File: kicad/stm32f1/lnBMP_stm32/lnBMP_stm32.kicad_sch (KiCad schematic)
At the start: 26 parts, among them J1 BMP Debug1, J2 BMP Debug2, J3 Debug port, J4 USB_OTG, U1 STM32F103CBTx, U2 LM1117-3.3, Y1 Crystal

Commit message: kicad : Update ch32 and stm32 pcbs
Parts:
- added DFU1: SW_DIP_x01, Button_Switch_SMD:SW_SPST_CK_RS282G05A3, symbol Switch:SW_DIP_x01
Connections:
- net NRESET is gone; now on net GND: J3.5 (Pin_5)
- net GND: now also DFU1.2; no longer J3.1 (Pin_1)
- net IN_FORCE_DFU: now also DFU1.1
- net SWDCLK: now also J3.4 (Pin_4); no longer J3.2 (Pin_2)
- net UART_TX: now also J3.2 (Pin_2); no longer J3.4 (Pin_4)
- net NRST: now reaches C1.1, R2.2, RST1.1, U1.7 (NRST)
- net NRST: now also J3.1 (Pin_1)
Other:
- moved on the sheet: J3
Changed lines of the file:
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@@
   (junction (at 265.43 24.13) (diameter 0) (color 0 0 0 0)
   )
+  (junction (at 50.8 62.23) (diameter 0) (color 0 0 0 0)
+  )
   (junction (at 252.73 31.75) (diameter 0) (color 0 0 0 0)
   )
@@
   (junction (at 74.93 62.23) (diameter 0) (color 0 0 0 0)
   )
+  (junction (at 48.26 130.81) (diameter 0) (color 0 0 0 0)
+  )
   (junction (at 13.97 72.39) (diameter 0) (color 0 0 0 0)
   )
@@
     (stroke (width 0) (type default))
   )
+  (wire (pts (xy 48.26 130.81) (xy 48.26 134.62))
+    (stroke (width 0) (type default))
+  )
   (wire (pts (xy 252.73 31.75) (xy 265.43 31.75))
     (stroke (width 0) (type default))
@@
     (stroke (width 0) (type default))
   )
+  (wire (pts (xy 55.88 50.8) (xy 55.88 62.23))
+    (stroke (width 0) (type default))
+  )
   (wire (pts (xy 144.78 146.05) (xy 144.78 149.86))
     (stroke (width 0) (type default))
@@
     (stroke (width 0) (type default))
   )
+  (wire (pts (xy 50.8 62.23) (xy 50.8 67.31))
+    (stroke (width 0) (type default))
+  )
   (wire (pts (xy 48.26 74.93) (xy 48.26 77.47))
     (stroke (width 0) (type default))
@@
     (stroke (width 0) (type default))
   )
+  (wire (pts (xy 48.26 130.81) (xy 52.07 130.81))
+    (stroke (width 0) (type default))
+  )
   (wire (pts (xy 102.87 36.83) (xy 106.68 36.83))
     (stroke (width 0) (type default))
@@
     (stroke (width 0) (type default))
   )
-  (wire (pts (xy 50.8 43.18) (xy 50.8 67.31))
+  (wire (pts (xy 55.88 62.23) (xy 50.8 62.23))
+    (stroke (width 0) (type default))
+  )
+  (wire (pts (xy 50.8 43.18) (xy 50.8 62.23))
     (stroke (width 0) (type default))
   )
@@
     (stroke (width 0) (type default))
   )
+  (wire (pts (xy 48.26 149.86) (xy 48.26 151.13))
+    (stroke (width 0) (type default))
+  )
   (wire (pts (xy 85.09 100.33) (xy 91.44 100.33))
     (stroke (width 0) (type default))
@@
     (stroke (width 0) (type default))
   )
-  (wire (pts (xy 46.99 130.81) (xy 52.07 130.81))
-    (stroke (width 0) (type default))
+  (wire (pts (xy 46.99 130.81) (xy 48.26 130.81))
+    (stroke (width 0) (type default))
+  )
+  (global_label "NRST" (shape input) (at 55.88 50.8 90) (fields_autoplaced)
+    (effects (font (size 1.27 1.27)) (justify left))
+    (property "Intersheetrefs" "${INTERSHEET_REFS}" (at 55.88 43.0372 90)
+      (effects (font (size 1.27 1.27)) (justify left) hide)
+    )
   )
   (global_label "SWDCLK" (shape input) (at 106.68 105.41 0) (fields_autoplaced)
@@
     )
   )
-  (global_label "NRESET" (shape input) (at 137.16 149.86 270) (fields_autoplaced)
-    (effects (font (size 1.27 1.27)) (justify right))
-    (property "Intersheetrefs" "${INTERSHEET_REFS}" (at 137.0806 159.3488 90)
+  (global_label "NRST" (shape input) (at 137.16 149.86 270) (fields_autoplaced)
+    (effects (font (size 1.27 1.27)) (justify right))
+    (property "Intersheetrefs" "${INTERSHEET_REFS}" (at 137.16 157.6228 90)
       (effects (font (size 1.27 1.27)) (justify right) hide)
     )
@@
     )
   )
+  (symbol (lib_id "Switch:SW_DIP_x01") (at 48.26 142.24 270) (unit 1)
+    (in_bom yes) (on_board yes) (dnp no) (fields_autoplaced)
+    (property "Reference" "DFU1" (at 52.07 140.97 90)
+      (effects (font (size 1.27 1.27)) (justify left))
+    )
+    (property "Value" "SW_DIP_x01" (at 52.07 143.51 90)
+      (effects (font (size 1.27 1.27)) (justify left))
+    )
+    (property "Footprint" "Button_Switch_SMD:SW_SPST_CK_RS282G05A3" (at 48.26 142.24 0)
+      (effects (font (size 1.27 1.27)) hide)
+    )
+    (property "Datasheet" "~" (at 48.26 142.24 0)
+      (effects (font (size 1.27 1.27)) hide)
+    )
+    (pin "1")
+    (pin "2")
+    (instances
+      (project "lnBMP_stm32"
+        (path "/fbe443d6-6d74-4abc-9dee-16e0160553bc"
+          (reference "DFU1") (unit 1)
+        )
+      )
+    )
+  )
   (symbol (lib_id "power:GND") (at 213.36 41.91 0) (unit 1)
     (in_bom yes) (on_board yes) (dnp no) (fields_autoplaced)
@@
     )
   )
+  (symbol (lib_id "power:GND") (at 48.26 151.13 0) (unit 1)
+    (in_bom yes) (on_board yes) (dnp no) (fields_autoplaced)
+    (property "Reference" "#PWR03" (at 48.26 157.48 0)
+      (effects (font (size 1.27 1.27)) hide)
+    )
+    (property "Value" "GND" (at 48.26 156.21 0)
+      (effects (font (size 1.27 1.27)))
+    )
+    (property "Footprint" "" (at 48.26 151.13 0)
+      (effects (font (size 1.27 1.27)) hide)
+    )
+    (property "Datasheet" "" (at 48.26 151.13 0)
+      (effects (font (size 1.27 1.27)) hide)
+    )
+    (pin "1")
+    (instances
+      (project "lnBMP_stm32"
+        (path "/fbe443d6-6d74-4abc-9dee-16e0160553bc"
+          (reference "#PWR03") (unit 1)
+        )
+      )
+    )
+  )
   (symbol (lib_id "Device:R_Small") (at 38.1 38.1 0) (unit 1)
     (in_bom yes) (on_board yes) (dnp no) (fields_autoplaced)
@@
     )
   )
-  (symbol (lib_id "Connector:Conn_01x05_Male") (at 142.24 140.97 270) (unit 1)
+  (symbol (lib_id "Connector:Conn_01x05_Male") (at 142.24 140.97 90) (mirror x) (unit 1)
     (in_bom yes) (on_board yes) (dnp no)
     (property "Reference" "J3" (at 142.24 135.89 90)
@@
       (effects (font (size 1.27 1.27)))
     )
-    (property "Footprint" "Connector_JST:JST_XH_B5B-XH-A_1x05_P2.50mm_Vertical" (at 143.51 165.1 90)
-      (effects (font (size 1.27 1.27)))
-    )
+    (property "Footprint" "Connector_JST:JST_XH_B5B-XH-A_1x05_P2.50mm_Vertical" (at 140.97 165.1 90)
+      (effects (font (size 1.27 1.27)))
+    )

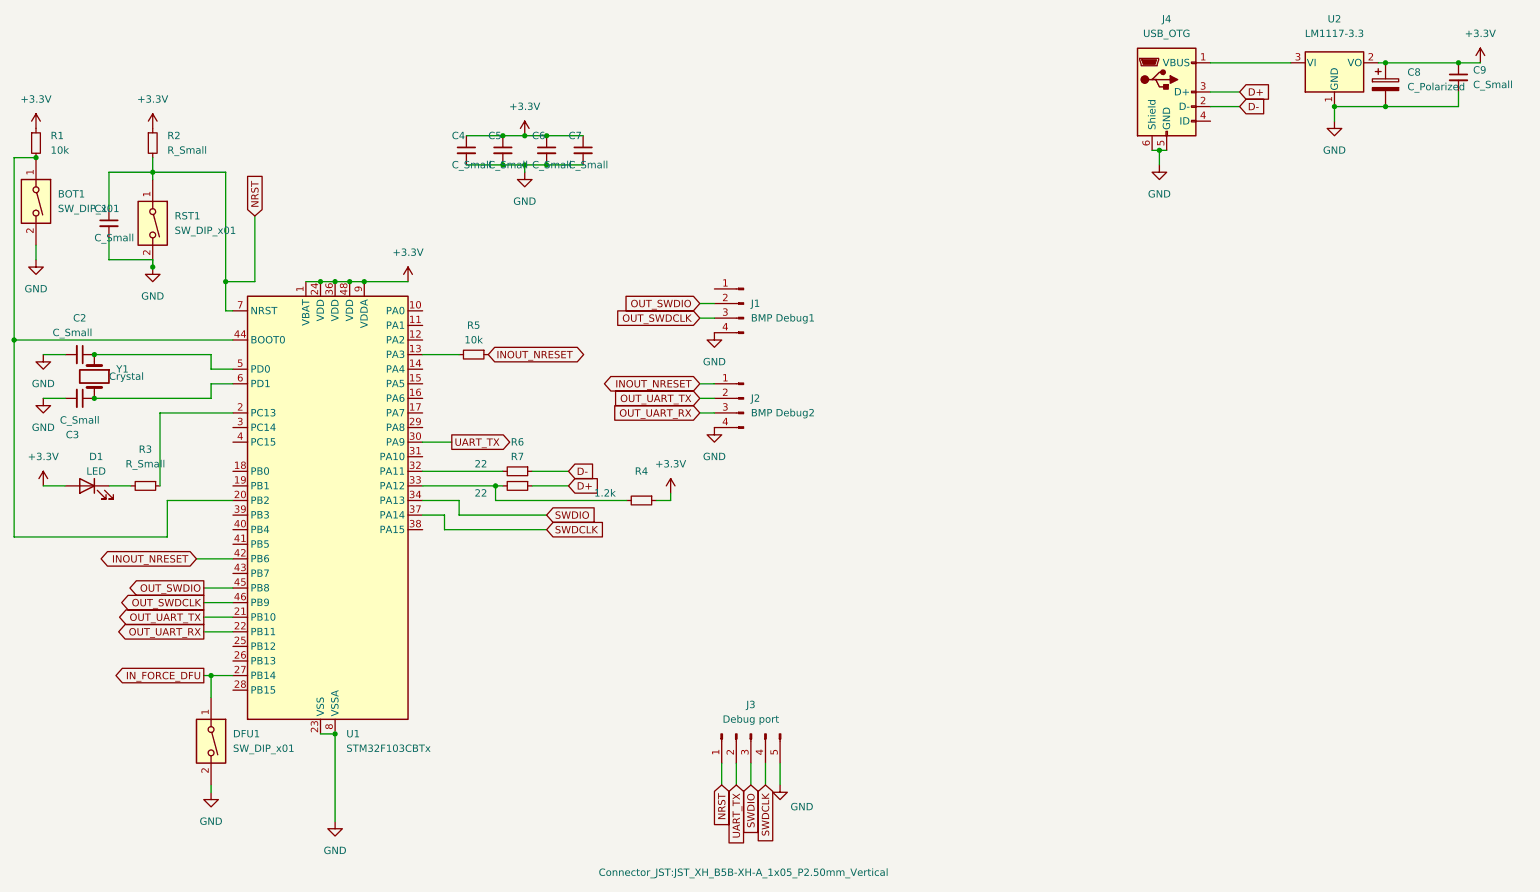
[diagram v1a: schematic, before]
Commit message: cleanup a bit the text + fix the inverted BOOT signal on stm32F1
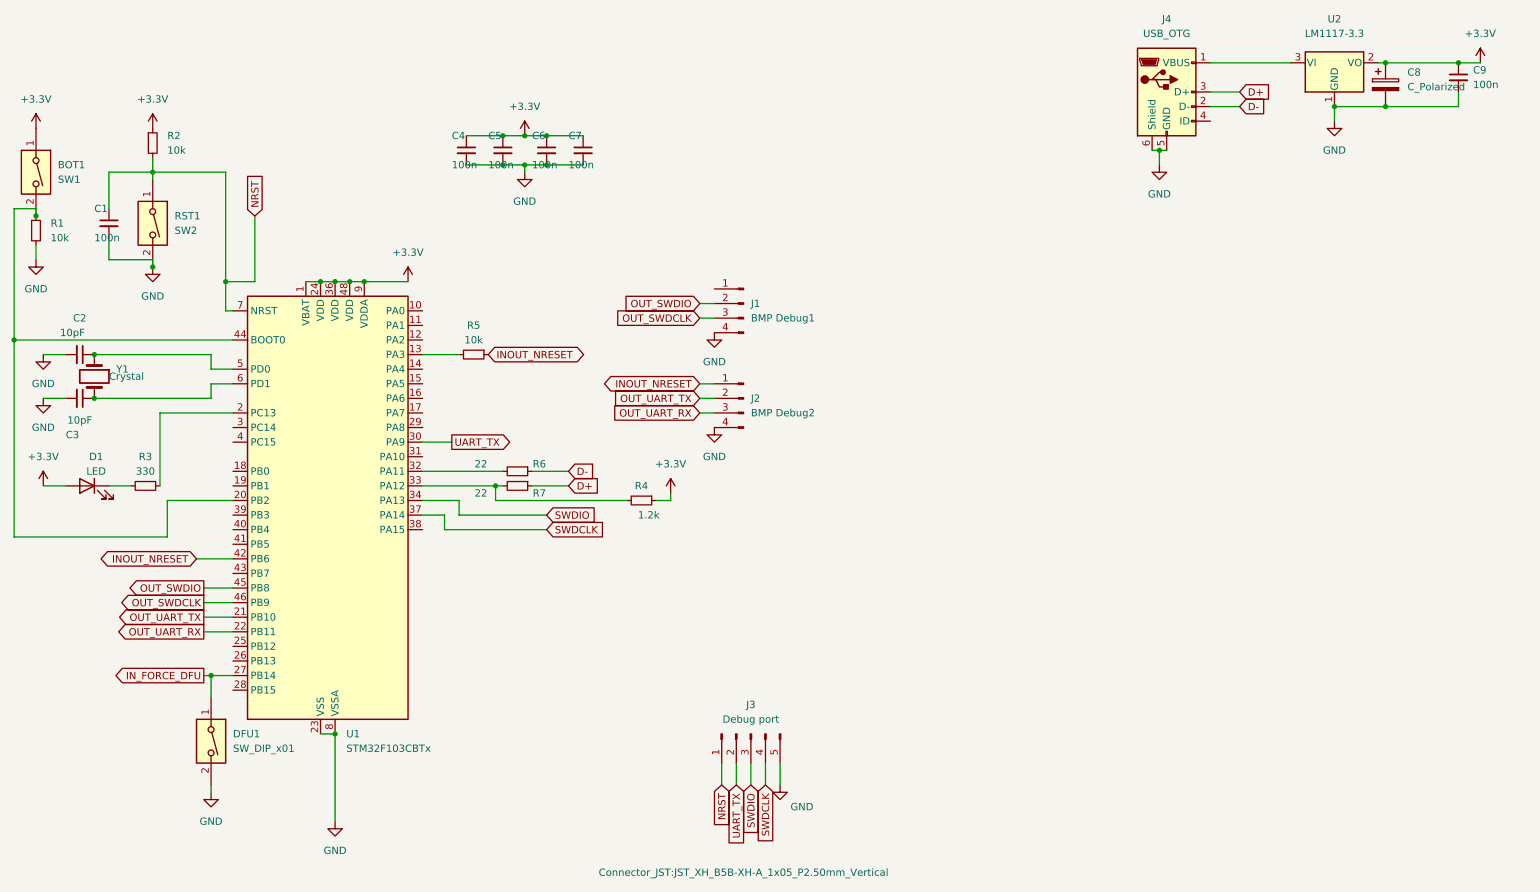
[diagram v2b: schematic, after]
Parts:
- BOT1: value SW_DIP_x01 -> SW1
- C1, C4, C5, C6, C7, C9: value C_Small -> 100n
- C2, C3: value C_Small -> 10pF
- R2: value R_Small -> 10k
- R3: value R_Small -> 330
- RST1: value SW_DIP_x01 -> SW2
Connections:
- net +3.3V: now also BOT1.1; no longer R1.1
- net GND: now also R1.2; no longer BOT1.2
- net at U1.20 (PB2), U1.44 (BOOT0): now also BOT1.2, R1.1; no longer BOT1.1, R1.2
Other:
- moved on the sheet: BOT1, R1

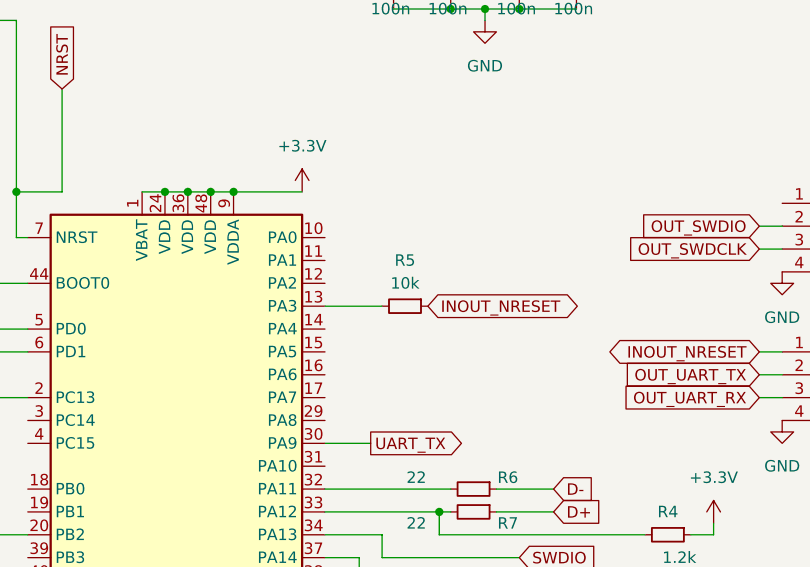
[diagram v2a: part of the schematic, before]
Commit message: stm32/gd32 : reduce rst input resistor, it acts as if a pulldown was behind
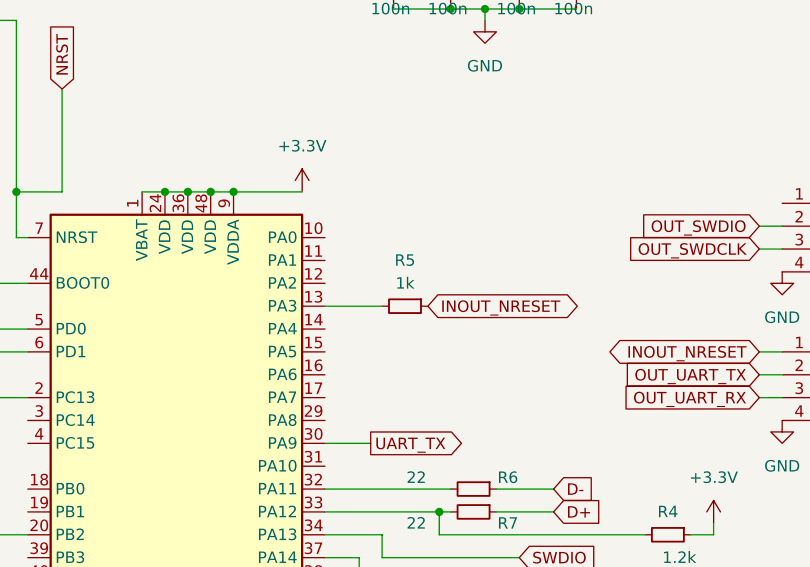
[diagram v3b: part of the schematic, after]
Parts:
- R5: value 10k -> 1k

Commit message: update lnArduino
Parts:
- added J5: Conn_ARM_JTAG_SWD_10, Connector_PinHeader_1.27mm:PinHeader_2x05_P1.27mm_Vertical_SMD, symbol Connector:Conn_ARM_JTAG_SWD_10
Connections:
- net GND: now also J5.3 (GND), J5.5 (GND), J5.9 (GNDDetect)
- net INOUT_NRESET: now also J5.10 (~{RESET})
- net OUT_SWDCLK: now also J5.4 (SWDCLK/TCK)
- net OUT_SWDIO: now also J5.2 (SWDIO/TMS)
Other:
- moved on the sheet: BOT1, C1, C2, C3, C4, C5, C6, C7, D1, DFU1, J1, J2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

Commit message: cleanup kicak / stm32
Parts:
- removed J5: Conn_ARM_JTAG_SWD_10, Connector_PinHeader_1.27mm:PinHeader_2x05_P1.27mm_Vertical_SMD, symbol Connector:Conn_ARM_JTAG_SWD_10
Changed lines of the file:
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@@
   (junction (at 86.36 72.39) (diameter 0) (color 0 0 0 0)
   )
-  (junction (at 54.61 127) (diameter 0) (color 0 0 0 0)
-  )
   (junction (at 157.48 26.67) (diameter 0) (color 0 0 0 0)
   )
@@
     (stroke (width 0) (type default))
   )
-  (wire (pts (xy 68.58 104.14) (xy 71.12 104.14))
-    (stroke (width 0) (type default))
-  )
   (wire (pts (xy 213.36 39.37) (xy 214.63 39.37))
     (stroke (width 0) (type default))
@@
     (stroke (width 0) (type default))
   )
-  (wire (pts (xy 53.34 127) (xy 54.61 127))
-    (stroke (width 0) (type default))
-  )
   (wire (pts (xy 109.22 52.07) (xy 109.22 57.15))
     (stroke (width 0) (type default))
@@
     (stroke (width 0) (type default))
   )
-  (wire (pts (xy 68.58 111.76) (xy 71.12 111.76))
-    (stroke (width 0) (type default))
-  )
   (wire (pts (xy 72.39 62.23) (xy 110.49 62.23))
     (stroke (width 0) (type default))
@@
     (stroke (width 0) (type default))
   )
-  (wire (pts (xy 54.61 127) (xy 55.88 127))
-    (stroke (width 0) (type default))
-  )
   (wire (pts (xy 72.39 39.37) (xy 76.2 39.37))
     (stroke (width 0) (type default))
@@
   )
   (wire (pts (xy 143.51 85.09) (xy 157.48 85.09))
-    (stroke (width 0) (type default))
-  )
-  (wire (pts (xy 68.58 109.22) (xy 71.12 109.22))
     (stroke (width 0) (type default))
   )
@@
     )
   )
-  (global_label "OUT_SWDIO" (shape input) (at 71.12 111.76 0) (fields_autoplaced)
-    (effects (font (size 1.27 1.27)) (justify left))
-    (property "Intersheetrefs" "${INTERSHEET_REFS}" (at 84.5676 111.76 0)
-      (effects (font (size 1.27 1.27)) (justify left) hide)
-    )
-  )
   (global_label "D-" (shape input) (at 168.91 85.09 0) (fields_autoplaced)
     (effects (font (size 1.27 1.27)) (justify left))
@@
     )
   )
-  (global_label "INOUT_NRESET" (shape input) (at 71.12 104.14 0) (fields_autoplaced)
-    (effects (font (size 1.27 1.27)) (justify left))
-    (property "Intersheetrefs" "${INTERSHEET_REFS}" (at 87.7123 104.14 0)
-      (effects (font (size 1.27 1.27)) (justify left) hide)
-    )
-  )
   (global_label "OUT_UART_RX" (shape input) (at 191.77 74.93 180) (fields_autoplaced)
     (effects (font (size 1.27 1.27)) (justify right))
@@
     )
   )
-  (global_label "OUT_SWDCLK" (shape input) (at 71.12 109.22 0) (fields_autoplaced)
-    (effects (font (size 1.27 1.27)) (justify left))
-    (property "Intersheetrefs" "${INTERSHEET_REFS}" (at 86.2004 109.22 0)
-      (effects (font (size 1.27 1.27)) (justify left) hide)
-    )
-  )
   (global_label "INOUT_NRESET" (shape bidirectional) (at 104.14 100.33 180) (fields_autoplaced)
     (effects (font (size 1.27 1.27)) (justify right))
@@
     )
   )
-  (symbol (lib_id "power:GND") (at 54.61 127 0) (unit 1)
-    (exclude_from_sim no) (in_bom yes) (on_board yes) (dnp no) (fields_autoplaced)
-    (property "Reference" "#PWR04" (at 54.61 133.35 0)
-      (effects (font (size 1.27 1.27)) hide)
-    )
-    (property "Value" "GND" (at 54.61 132.08 0)
-      (effects (font (size 1.27 1.27)))
-    )
-    (property "Footprint" "" (at 54.61 127 0)
-      (effects (font (size 1.27 1.27)) hide)
-    )
-    (property "Datasheet" "" (at 54.61 127 0)
-      (effects (font (size 1.27 1.27)) hide)
-    )
-    (property "Description" "" (at 54.61 127 0)
-      (effects (font (size 1.27 1.27)) hide)
-    )
-    (pin "1")
-    (instances
-      (project "lnBMP_stm32"
-        (path "/fbe443d6-6d74-4abc-9dee-16e0160553bc"
-          (reference "#PWR04") (unit 1)
-        )
-      )
-    )
-  )
   (symbol (lib_id "Device:C_Small") (at 165.1 29.21 0) (unit 1)
     (exclude_from_sim no) (in_bom yes) (on_board yes) (dnp no)
@@
         )
       )
-    )
-  )
-  (symbol (lib_id "Connector:Conn_ARM_JTAG_SWD_10") (at 55.88 111.76 0) (unit 1)
-    (exclude_from_sim no) (in_bom yes) (on_board yes) (dnp no) (fields_autoplaced)
-    (property "Reference" "J5" (at 44.45 110.4899 0)
-      (effects (font (size 1.27 1.27)) (justify right))
-    )
-    (property "Value" "Conn_ARM_JTAG_SWD_10" (at 44.45 113.0299 0)
-      (effects (font (size 1.27 1.27)) (justify right))
-    )
-    (property "Footprint" "Connector_PinHeader_1.27mm:PinHeader_2x05_P1.27mm_Vertical_SMD" (at 55.88 111.76 0)
-      (effects (font (size 1.27 1.27)) hide)
-    )
-    (property "Datasheet" "http://infocenter.arm.com/help/topic/com.arm.doc.ddi0314h/DDI0314H_coresight_components_trm.pdf" (at 46.99 143.51 90)
-      (effects (font (size 1.27 1.27)) hide)
-    )
-    (property "Description" "Cortex Debug Connector, standard ARM Cortex-M SWD and JTAG interface" (at 55.88 111.76 0)
-      (effects (font (size 1.27 1.27)) hide)
-    )
-    (pin "8")
-    (pin "7")
-    (pin "9")
-    (pin "4")
-    (pin "5")
-    (pin "1")
-    (pin "6")
-    (pin "2")
-    (pin "10")
-    (pin "3")
-    (instances
-      (project "lnBMP_stm32"
-        (path "/fbe443d6-6d74-4abc-9dee-16e0160553bc"
-          (reference "J5") (unit 1)
-        )
-      )
